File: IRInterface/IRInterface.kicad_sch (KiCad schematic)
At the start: 26 parts, among them IC1 THVD1424RGTR, J1 USB_B_Micro, J2 RJHSE5E80, J3 FTSH-105-01-L-DV-007-K, Q1 SFH309, Q2 BC817, Q3 BC807, U1 74LVC1G17, U2 74LVC1G17, U3 STM32G030F6Px

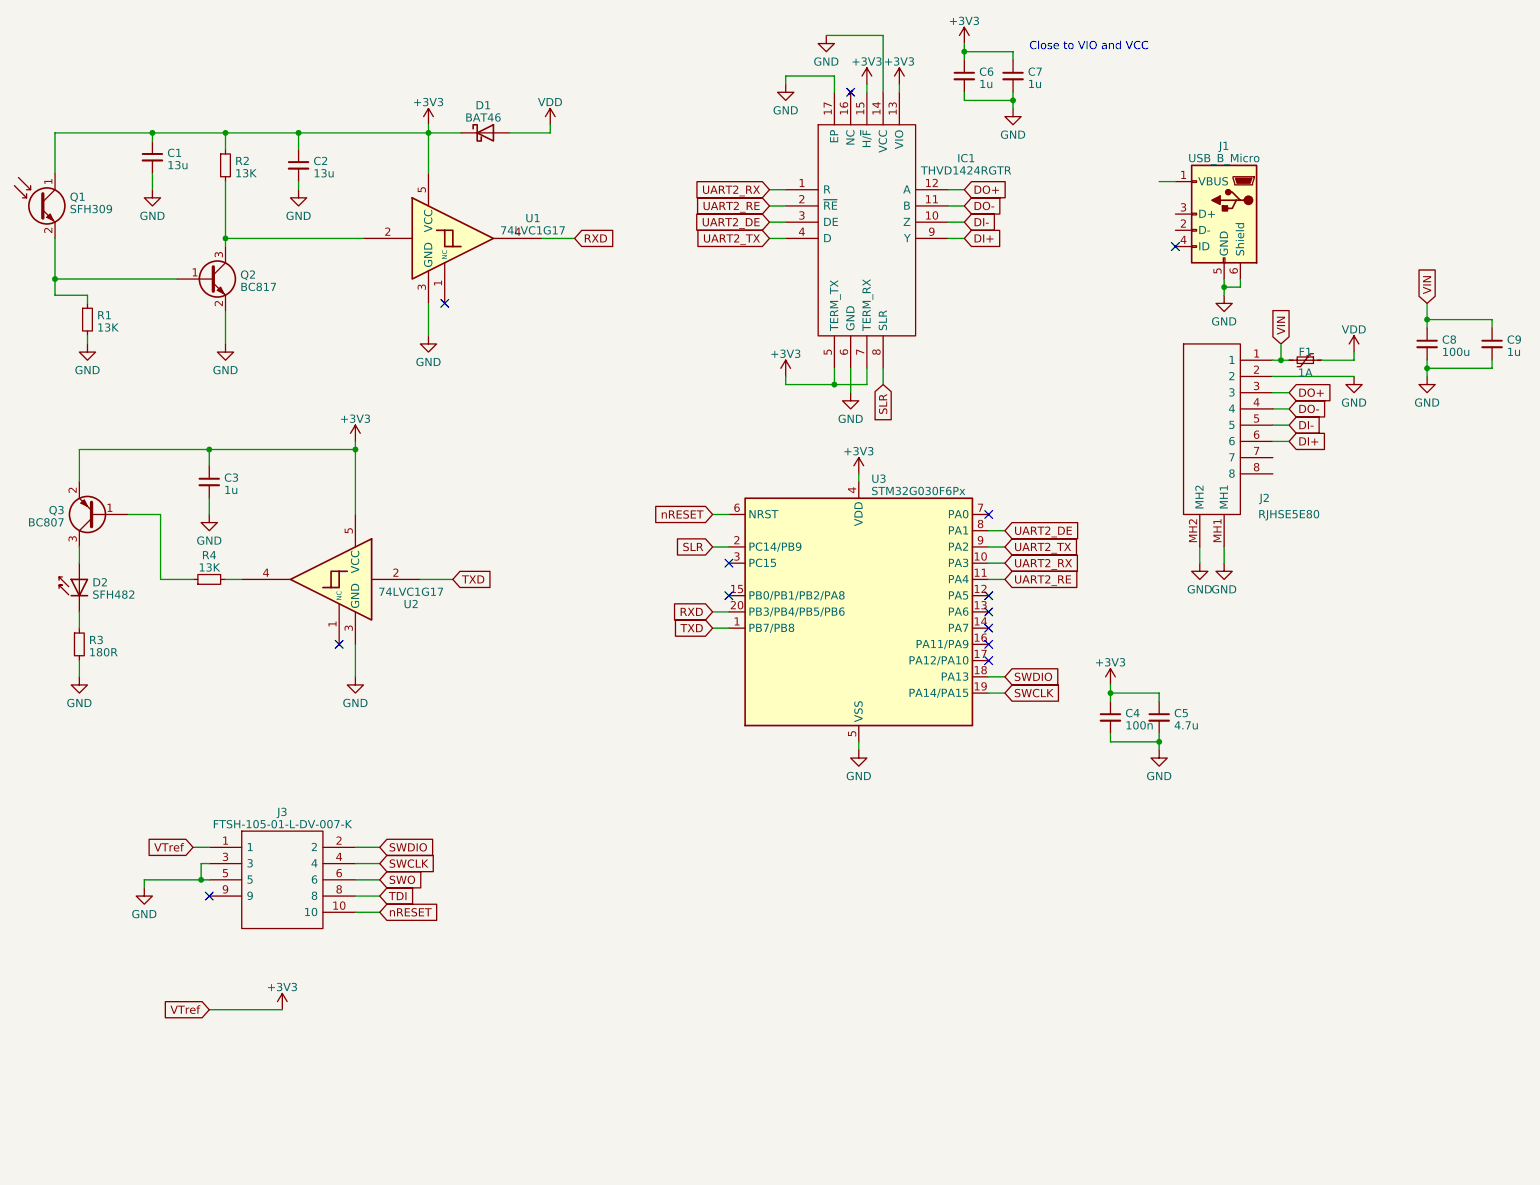
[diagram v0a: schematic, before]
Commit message: Added Symbol libraries and restructure schematic
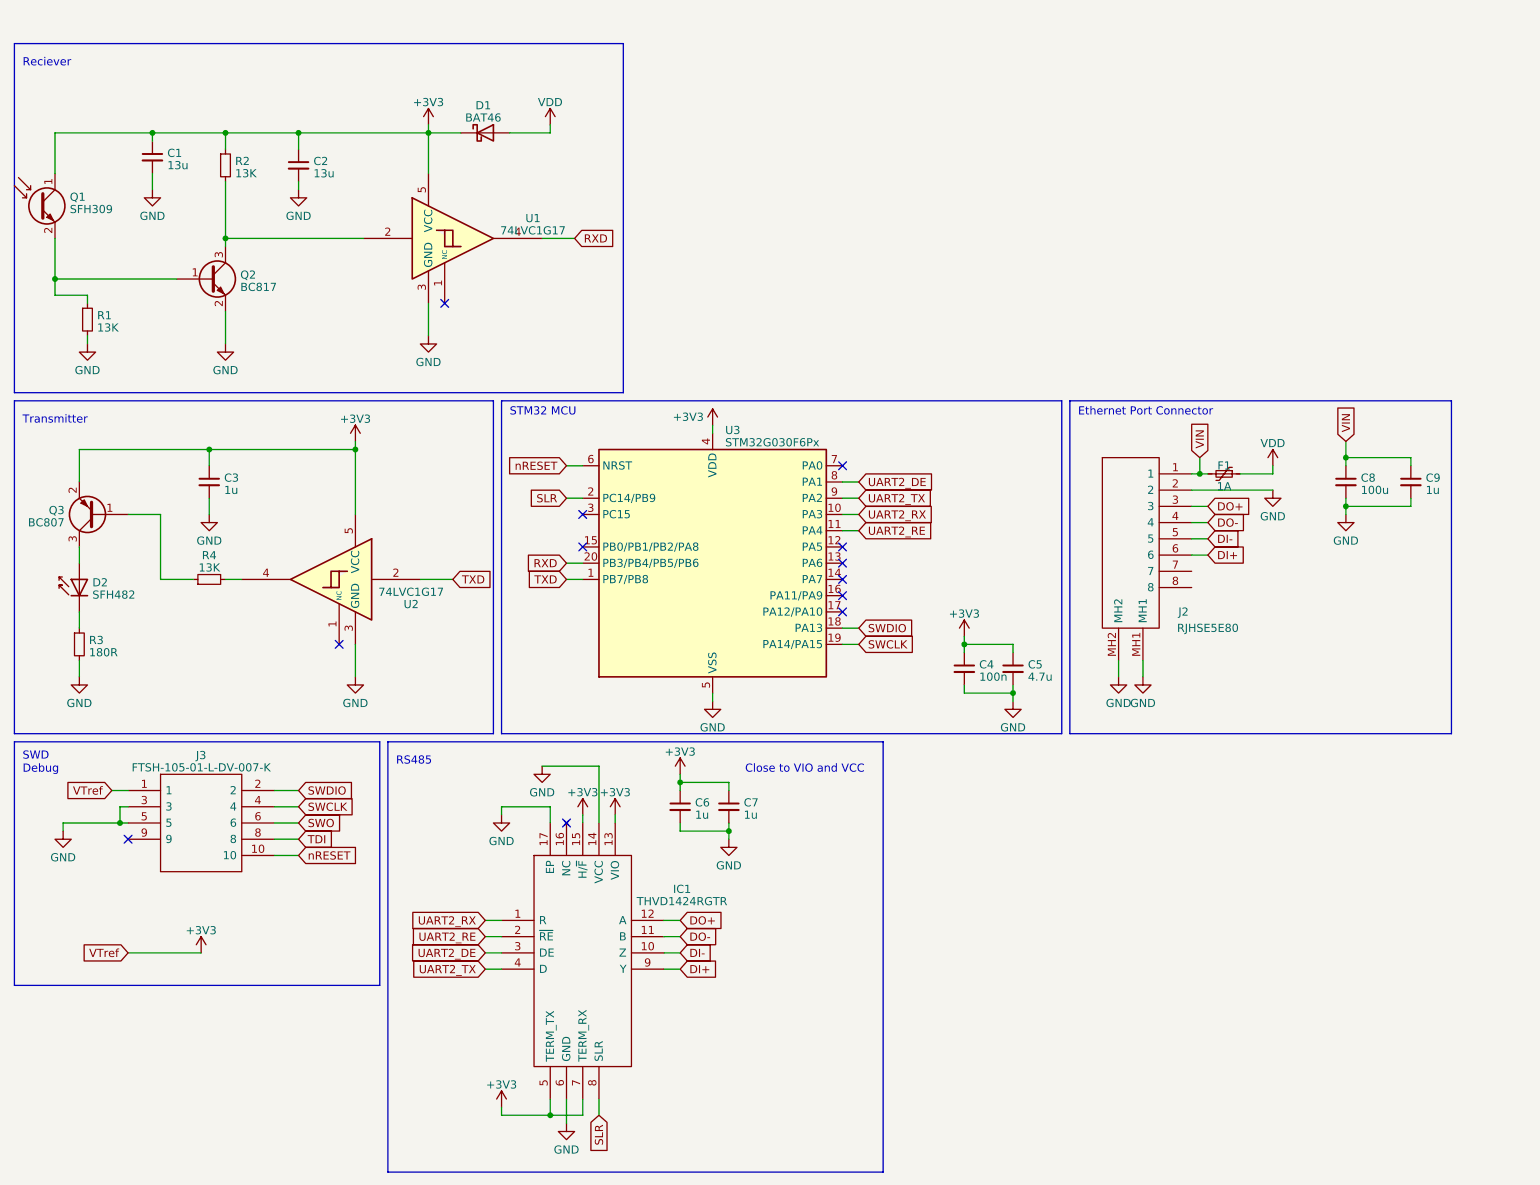
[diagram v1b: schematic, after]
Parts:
- removed J1: USB_B_Micro, symbol Connector:USB_B_Micro
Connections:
- no-connect marks 13 -> 12
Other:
- note added: "Ethernet Port Connector"
- note added: "RS485"
- note added: "Reciever"
- note added: "STM32 MCU"
- note added: "SWD Debug"
- note added: "Transmitter"
- moved on the sheet: C4, C5, C6, C7, C8, C9, F1, IC1, J2, J3, U3

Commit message: Fix review findings
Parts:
- R3: value 180R -> 150R
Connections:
- net +3V3: now also IC1.14 (VCC); no longer IC1.15 (H/~{F})
- net GND: now also IC1.15 (H/~{F}); no longer IC1.14 (VCC)
- no-connect marks 12 -> 14
